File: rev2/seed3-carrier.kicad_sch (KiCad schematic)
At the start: 84 parts, among them J1 AudioJack2_Switch, J2 AudioJack2, J3 POWER_BOARD, J4 DISPLAY_UART, J5 SJ3-35063AG, J6 Seed3_PINS_RIGHT, J7 Seed3_PINS_LEFT, Q1 AO3401A, Q2 2N7002, Q3 2N7002, Q4 2N7002, SW1 EC11E, U1 TLV9064IDR, U2 TPA6111A2DR, U3 SN74LVC1G123DCTR

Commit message: Add J8 internal line out to the speaker amp
- Add J8, a 2-pin JST-XH (B2B-XH-A): pin 1 on J2's tip after R3,
  now named LINE_OUT, and pin 2 on GND. It feeds the speaker amp on
  the power board or a class D module while prototyping.
- Keep J2 as an external line out on the same net.
- Document J8, cabling and speaker wiring in rev2/CHANGES.md.

Co-Authored-By: Claude Opus 5.5 <noreply@anthropic.com>
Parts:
- added J8: LINE_OUT, Connector_JST:JST_XH_B2B-XH-A_1x02_P2.50mm_Vertical, symbol Connector_Generic:Conn_01x02
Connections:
- net GND: now also J8.2 (Pin_2)
- net LINE_OUT: now reaches J2.T, R3.1, R4.2
- net LINE_OUT: now also J8.1 (Pin_1)
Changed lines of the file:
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@@
+		)
+	)
+	(wire
+		(pts
+			(xy 223.52 43.18) (xy 223.52 38.1)
+		)
+		(stroke
+			(width 0)
+			(type default)
+		)
+	)
+	(label "LINE_OUT"
+		(at 223.52 38.1 90)
+		(effects
+			(font
+				(size 1.27 1.27)
+			)
+			(justify left bottom)
+		)
+	)
+	(symbol
+		(lib_id "Connector_Generic:Conn_01x02")
+		(at 264.16 48.26 0)
+		(unit 1)
+		(body_style 1)
+		(exclude_from_sim no)
+		(in_bom yes)
+		(on_board yes)
+		(in_pos_files yes)
+		(dnp no)
+		(property "Reference" "J8"
+			(at 264.16 45.72 0)
+			(show_name no)
+			(do_not_autoplace no)
+			(effects
+				(font
+					(size 1.27 1.27)
+				)
+				(justify left)
+			)
+		)
+		(property "Value" "LINE_OUT"
+			(at 264.16 53.34 0)
+			(show_name no)
+			(do_not_autoplace no)
+			(effects
+				(font
+					(size 1.27 1.27)
+				)
+				(justify left)
+			)
+		)
+		(property "Footprint" "Connector_JST:JST_XH_B2B-XH-A_1x02_P2.50mm_Vertical"
+			(at 264.16 48.26 0)
+			(hide yes)
+			(show_name no)
+			(do_not_autoplace no)
+			(effects
+				(font
+					(size 1.27 1.27)
+				)
+			)
+		)
+		(property "Datasheet" ""
+			(at 264.16 48.26 0)
+			(hide yes)
+			(show_name no)
+			(do_not_autoplace no)
+			(effects
+				(font
+					(size 1.27 1.27)
+				)
+			)
+		)
+		(property "Description" "Generic connector, single row, 01x02, script generated (kicad-library-utils/schlib/autogen/connector/)"
+			(at 264.16 48.26 0)
+			(hide yes)
+			(show_name no)
+			(do_not_autoplace no)
+			(effects
+				(font
+					(size 1.27 1.27)
+				)
+			)
+		)
+		(pin "1"
+		)
+		(pin "2"
+		)
+		(pin "4")
+		(instances
+			(project "seed3-carrier"
+				(path "/94ecceca-f8ce-4e68-9c84-99ac5115dfb9"
+					(reference "J8")
+					(unit 1)
+				)
+			)
+		)
+	)
+	(label "LINE_OUT"
+		(at 259.08 48.26 180)
+		(effects
+			(font
+				(size 1.27 1.27)
+			)
+			(justify right bottom)
+		)
+	)
+	(wire
+		(pts
+			(xy 259.08 50.8) (xy 256.54 50.8)
+		)
+		(stroke
+			(width 0)
+			(type default)
+		)
+	)
+	(wire
+		(pts
+			(xy 256.54 50.8) (xy 256.54 53.34)
+		)
+		(stroke
+			(width 0)
+			(type default)
+		)
+	)
+	(symbol
+		(lib_id "power:GND")
+		(at 256.54 53.34 0)
+		(unit 1)
+		(body_style 1)
+		(exclude_from_sim no)
+		(in_bom yes)
+		(on_board yes)
+		(in_pos_files yes)
+		(dnp no)
+		(property "Reference" "#PWR058"
+			(at 256.54 53.34 0)
+			(hide yes)
+			(show_name no)
+			(do_not_autoplace no)
+			(effects
+				(font
+					(size 1.27 1.27)
+				)
+			)
+		)
+		(property "Value" "GND"
+			(at 256.54 58.42 0)
+			(show_name no)
+			(do_not_autoplace no)
+			(effects
+				(font
+					(size 1.27 1.27)
+				)
+			)
+		)
+		(property "Footprint" ""
+			(at 256.54 53.34 0)
+			(hide yes)
+			(show_name no)
+			(do_not_autoplace no)
+			(effects
+				(font
+					(size 1.27 1.27)
+				)
+			)
+		)
+		(property "Datasheet" ""
+			(at 256.54 53.34 0)
+			(hide yes)
+			(show_name no)
+			(do_not_autoplace no)
+			(effects
+				(font
+					(size 1.27 1.27)
+				)
+			)
+		)
+		(property "Description" "Power symbol creates a global label with name \"GND\" , ground"
+			(at 256.54 53.34 0)
+			(hide yes)
+			(show_name no)
+			(do_not_autoplace no)
+			(effects
+				(font
+					(size 1.27 1.27)
+				)
+			)
+		)
+		(pin "1"
+		)
+		(instances
+			(project "seed3-carrier"
+				(path "/94ecceca-f8ce-4e68-9c84-99ac5115dfb9"
+					(reference "#PWR058")
+					(unit 1)
+				)
+			)
 		)
 	)

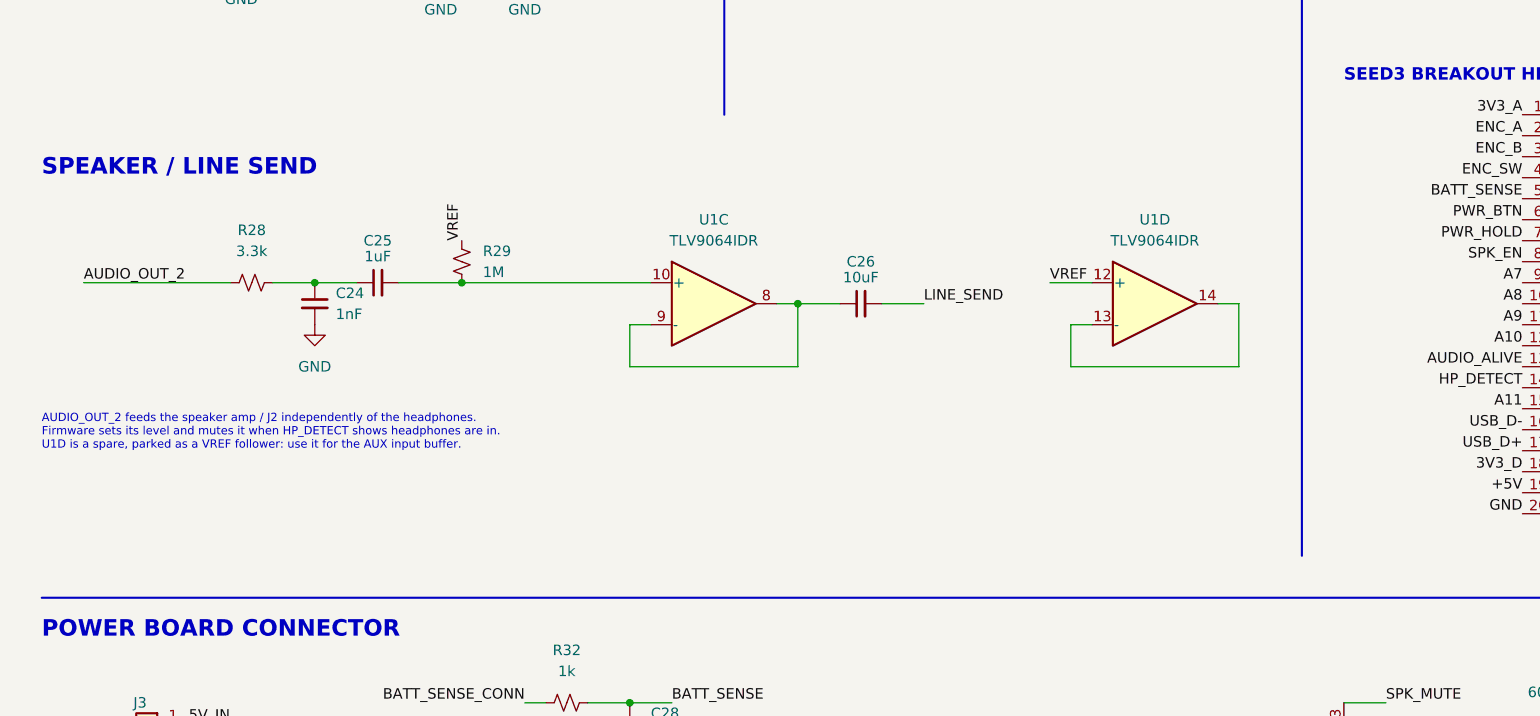
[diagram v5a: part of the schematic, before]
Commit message: Add the AUX input on J9 through U1D to AUDIO_IN_2
- Add J9, a second SJ3-35063AG 3.5 mm TRS jack. Its detect switch
  is not connected.
- Sum tip and ring to mono with R40/R41 (10k), hold the node with
  R38 (47k) and C31 (1nF), AC-couple with C32 (1uF) biased to VREF
  by R39 (100k), then R42 (1k) into the U1D follower driving
  AUDIO_IN_2.
- Remove U1D's VREF-follower parking and move it next to the AUX
  parts. Rename the section to "Speaker / line send, AUX input".
- Document the path, firmware mixing and the level check in
  rev2/CHANGES.md.

Co-Authored-By: Claude Opus 5.5 <noreply@anthropic.com>
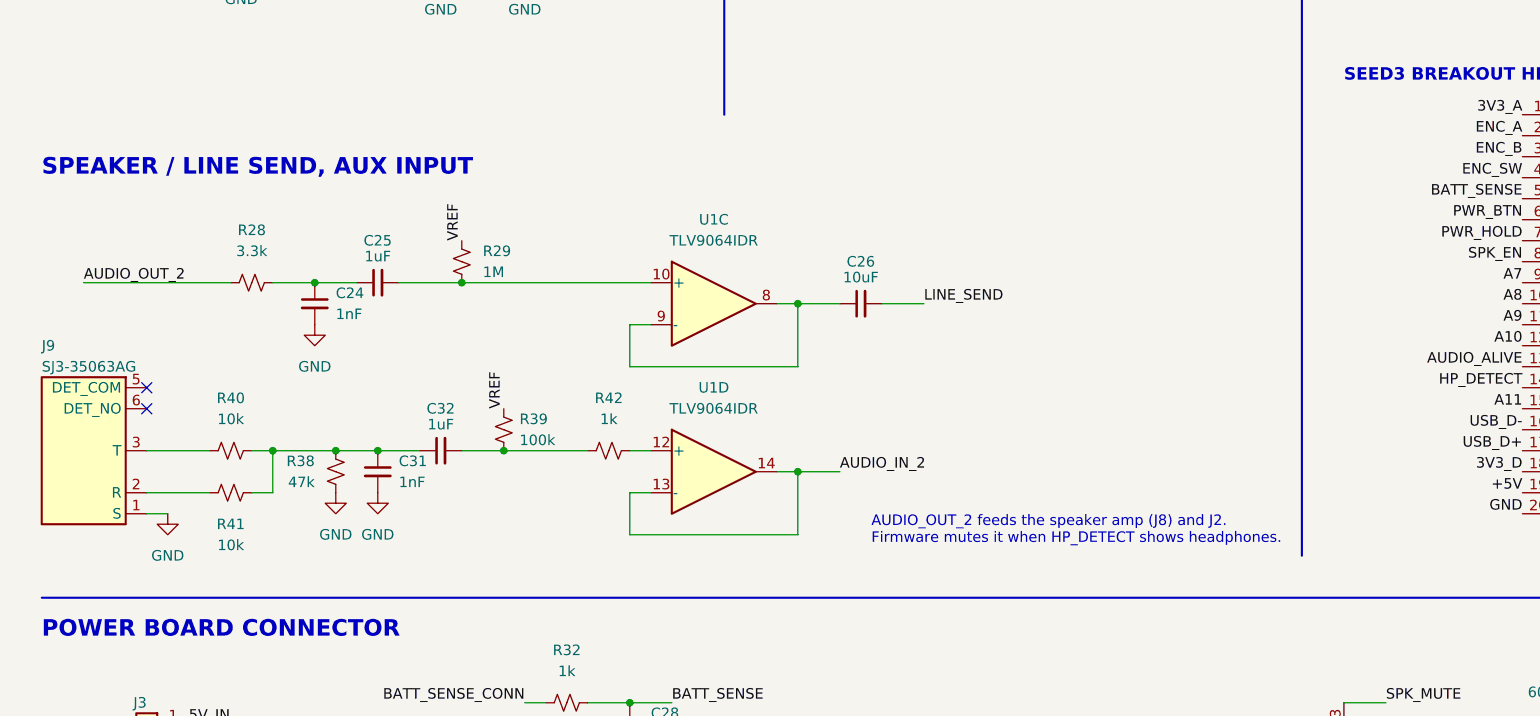
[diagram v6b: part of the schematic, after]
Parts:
- added C31: 1nF, Capacitor_SMD:C_1206_3216Metric_Pad1.33x1.80mm_HandSolder, symbol Device:C_Small
- added C32: 1uF, Capacitor_SMD:C_1206_3216Metric_Pad1.33x1.80mm_HandSolder, symbol Device:C_Small
- added J9: SJ3-35063AG, Seed3_Carrier:Jack_3.5mm_SameSky_SJ3-35063AG_Horizontal, symbol seed3-carrier:SJ3-35063AG
- added R38: 47k, Resistor_SMD:R_1206_3216Metric_Pad1.30x1.75mm_HandSolder, symbol Device:R_Small_US
- added R39: 100k, Resistor_SMD:R_1206_3216Metric_Pad1.30x1.75mm_HandSolder, symbol Device:R_Small_US
- added R40, R41: 10k, Resistor_SMD:R_1206_3216Metric_Pad1.30x1.75mm_HandSolder, symbol Device:R_Small_US
- added R42: 1k, Resistor_SMD:R_1206_3216Metric_Pad1.30x1.75mm_HandSolder, symbol Device:R_Small_US
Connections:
- net AUDIO_IN_2: now also U1.13 (-), U1.14
- net GND: now also C31.2, J9.1 (S), R38.2
- net VREF: now also R39.1; no longer U1.12 (+)
- new net: J9.2 (R), R41.1
- new net: C31.1, C32.1, R38.1, R40.2, R41.2
- new net: J9.3 (T), R40.1
- new net: C32.2, R39.2, R42.1
- new net: R42.2, U1.12 (+)
- no-connect marks 1 -> 3
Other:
- note added: "AUDIO_OUT_2 feeds the speaker amp (J8) and J2. Firmware mutes it when HP_DETECT shows headphones."
- note added: "SPEAKER / LINE SEND, AUX INPUT"
- note removed: "AUDIO_OUT_2 feeds the speaker amp / J2 independently of the headphones. Firmware sets its level and mutes it when HP_DETECT shows headphones are in. U1D is a spare, parked as a VREF follower: use it for the AUX input buffer."
- note removed: "SPEAKER / LINE SEND"
- moved on the sheet: U1D

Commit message: Apply rev 2 schematic design review fixes
Technical:
- R32 1k -> 10k so the power board's battery divider cannot
  back-power an unpowered Daisy through BATT_SENSE.
- R13/R14 100R -> 1k: now only bleed resistors for C14/C15 since
  the rev 1 tip-switch line out is gone.
- Add R43/R44 (1k) in series with the display UART. J4 now carries
  UART_TX_CONN/UART_RX_CONN.

Style:
- Add voltage ratings to C7, C9, C26 and C30. Rename TP9 to TP_5V.
- Rename "Audio output" to "Headphone buffer" and update the Q1,
  op-amp rail and watchdog notes. Update the title block date.
- Move C9's labels clear of the PWR_FLAG symbols.
- Record the fixes and the BATT_SENSE power board requirement in
  rev2/CHANGES.md.

Co-Authored-By: Claude Opus 5.5 <noreply@anthropic.com>
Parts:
- added R43, R44: 1k, Resistor_SMD:R_1206_3216Metric_Pad1.30x1.75mm_HandSolder, symbol Device:R_Small_US
- C26, C9: value 10uF -> 10uF 16V
- C30: value 47uF -> 47uF 16V
- C7: value 47uF -> 47uF 10V
- R13, R14: value 100 -> 1k
- R32: value 1k -> 10k
- TP9: value TP_AMP_5V -> TP_5V
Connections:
- net DISPLAY_UART_RX: now also R44.2; no longer J4.3 (Pin_3)
- net DISPLAY_UART_TX: now also R43.1; no longer J4.2 (Pin_2)
- new net UART_RX_CONN: J4.3 (Pin_3), R44.1
- new net UART_TX_CONN: J4.2 (Pin_2), R43.2
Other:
- note added: "HEADPHONE BUFFER"
- note added: "Op-amp power rails"
- note added: "Q1: reverse-polarity protection for 5V_IN (J3)"
- note added: "U2 stays muted (SHUTDOWN pulled to +5V) unless the firmware toggles AUDIO_ALIVE from the audio callback. Each rising edge retriggers U3; if edges stop for ~10 ms (Rext x Cext), Q (WD_OK) falls: Q2 mutes U2 and Q3 mutes the speaker amp. Also muted while the Daisy is absent, booting or in DFU (B is held low). The speaker amp mute is SPK_MUTE on J3."
- note removed: "AUDIO OUTPUT"
- note removed: "MOSFET is reverse polarity protection"
- note removed: "OPAMP power rails"
- note removed: "U2 stays muted (SHUTDOWN pulled to +5V) unless the firmware toggles AUDIO_ALIVE from the audio callback. Each rising edge retriggers U3; if edges stop for ~10 ms (Rext x Cext), Q falls, Q2 turns off and the amps mute. Also muted while the Daisy is absent, booting or in DFU (B is held low). AMP_SHUTDOWN mutes U2; the speaker amp uses SPK_MUTE on J3."

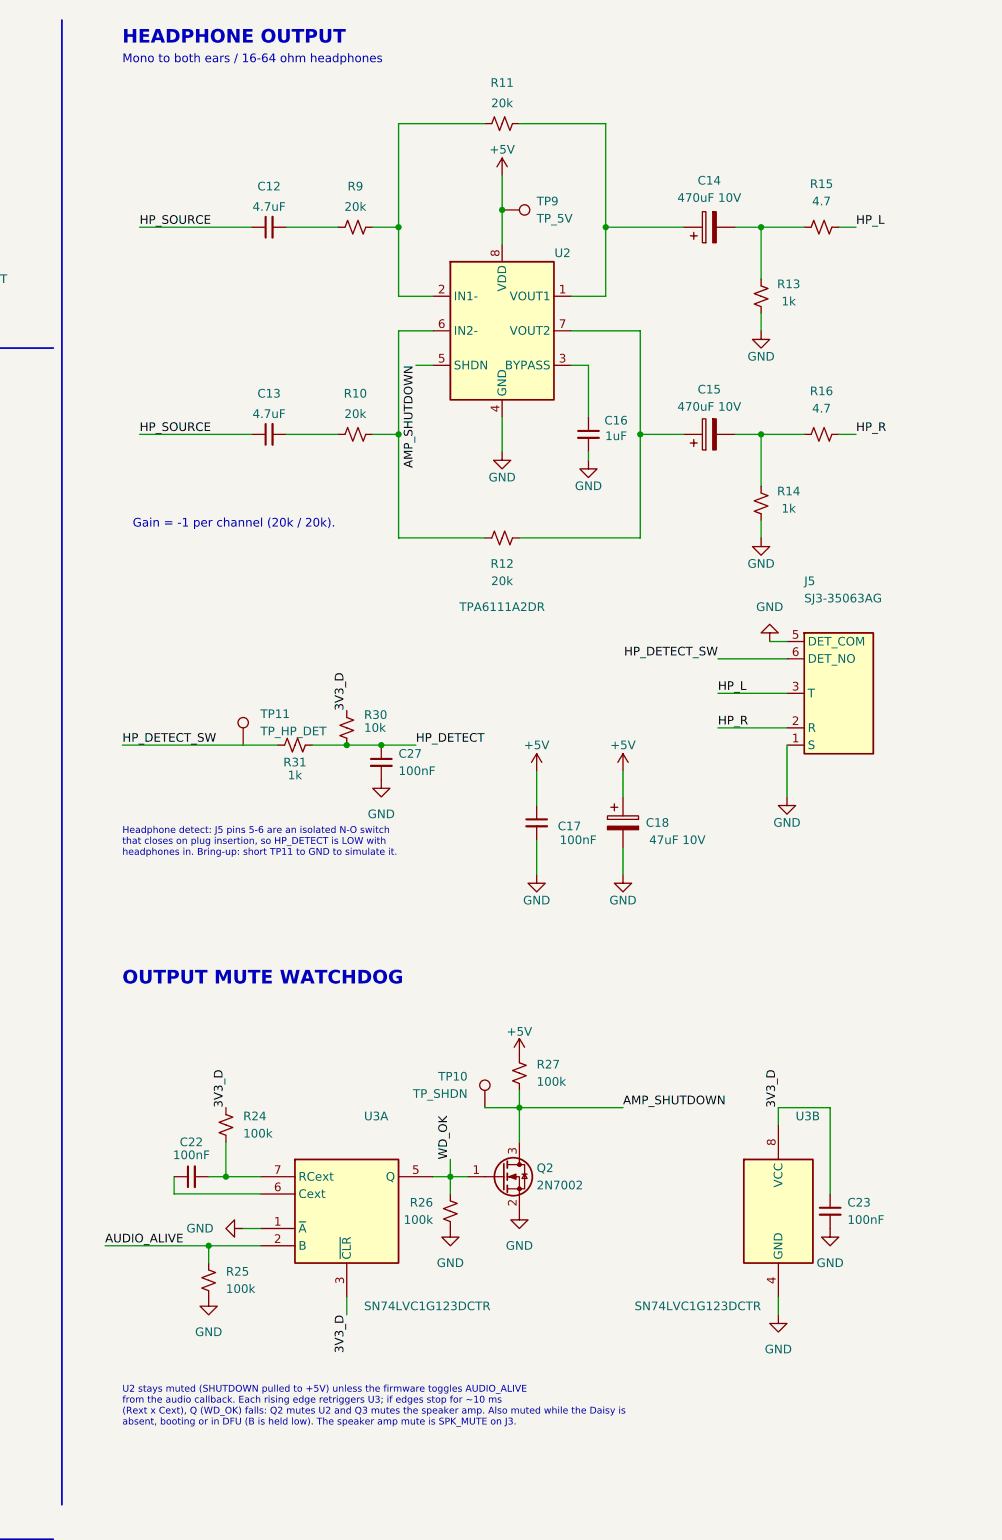
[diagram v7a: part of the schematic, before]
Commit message: Replace the TPA6111A2 headphone amp with a TPA6132A2
- U2 is now a TPA6132A2RTE DirectPath amp (WQFN-16). Its outputs sit
  at 0 V and drive J5 directly.
- Remove C14/C15 (470uF output caps), R9-R16, C16, Q2 and R27.
- Add C33 (VDD), C34 (HPVDD), C35 (flying) and C36 (HPVSS) per the
  datasheet. Inputs are single ended through C12/C13, and gain is
  0 dB (G0 high, G1 low).
- Drive U2's active-high EN straight from WD_OK, replacing
  AMP_SHUTDOWN. Move TP10 onto WD_OK.
- Add a TPA6132A2RTE symbol with pins arranged for this circuit to
  seed3-carrier.kicad_sym.
- Update rev2/CHANGES.md: the watchdog, the power connector and
  firmware notes, open items, and a new section for the swap.

Co-Authored-By: Claude Opus 5.5 <noreply@anthropic.com>
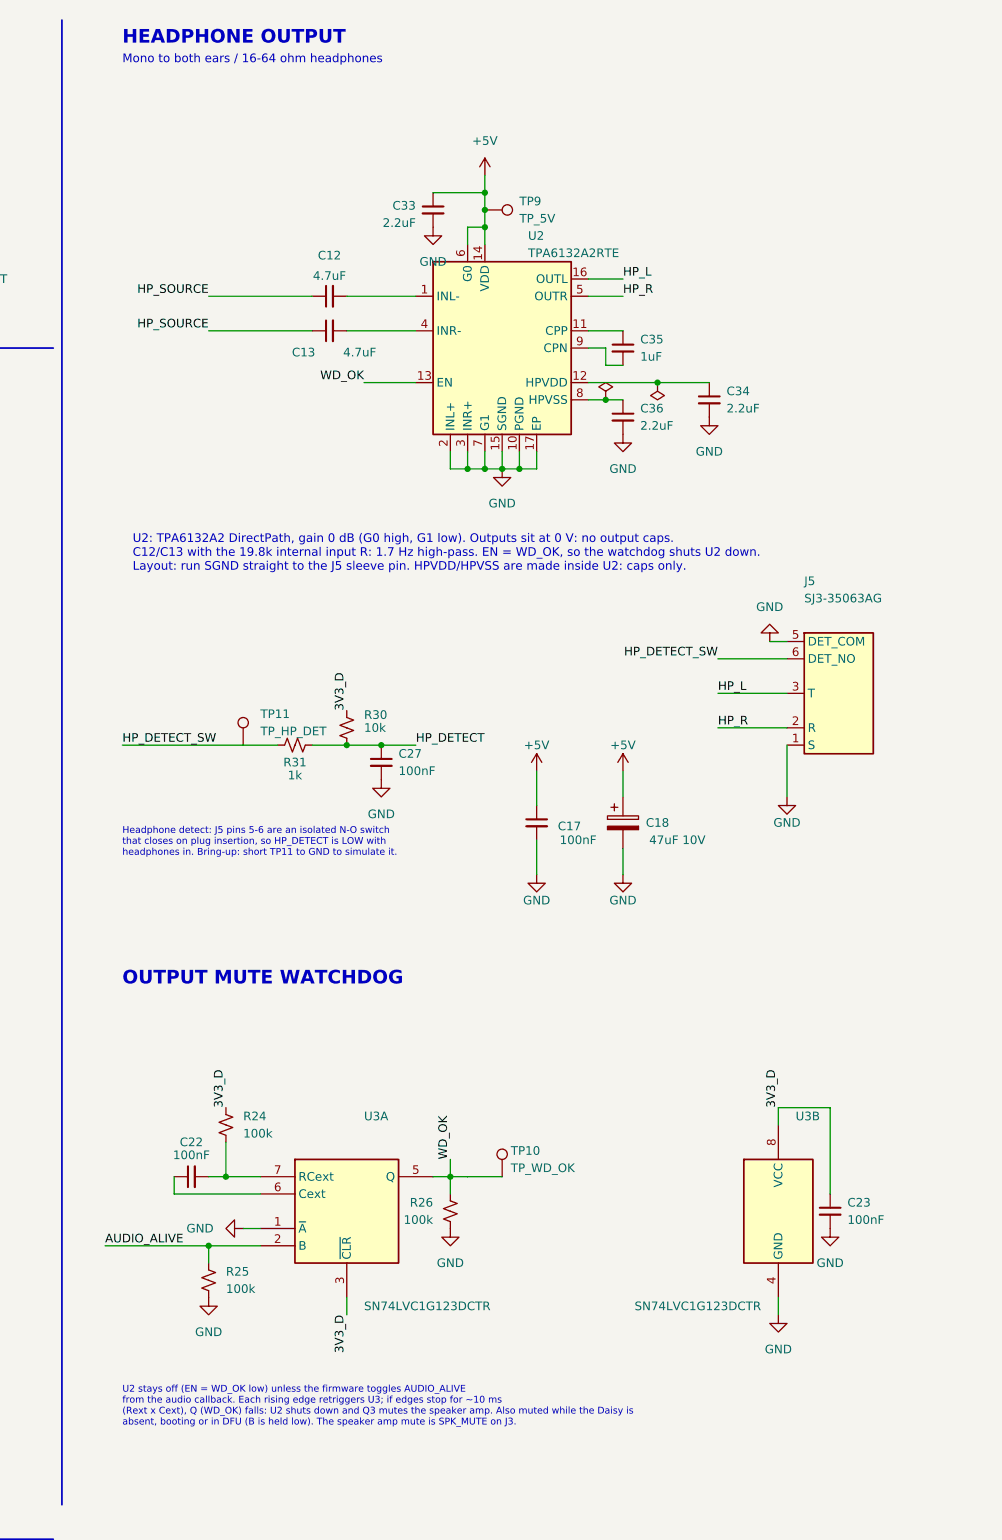
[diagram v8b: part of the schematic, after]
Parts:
- removed C14, C15: 470uF 10V, Capacitor_THT:CP_Radial_D8.0mm_P3.50mm, symbol Device:C_Polarized
- removed C16: 1uF, Capacitor_SMD:C_1206_3216Metric_Pad1.33x1.80mm_HandSolder, symbol Device:C_Small
- removed Q2: 2N7002, Package_TO_SOT_SMD:SOT-23, symbol Transistor_FET:2N7002
- removed R10, R11, R12, R9: 20k, Resistor_SMD:R_1206_3216Metric_Pad1.30x1.75mm_HandSolder, symbol Device:R_Small_US
- removed R13, R14: 1k, Resistor_SMD:R_1206_3216Metric_Pad1.30x1.75mm_HandSolder, symbol Device:R_Small_US
- removed R15, R16: 4.7, Resistor_SMD:R_1206_3216Metric_Pad1.30x1.75mm_HandSolder, symbol Device:R_Small_US
- removed R27: 100k, Resistor_SMD:R_1206_3216Metric_Pad1.30x1.75mm_HandSolder, symbol Device:R_Small_US
- removed U2: TPA6111A2DR, Package_SO:SOIC-8_3.9x4.9mm_P1.27mm, symbol seed3-carrier:TPA6111A2DR
- added C33, C34, C36: 2.2uF, Capacitor_SMD:C_0805_2012Metric_Pad1.18x1.45mm_HandSolder, symbol Device:C_Small
- added C35: 1uF, Capacitor_SMD:C_0805_2012Metric_Pad1.18x1.45mm_HandSolder, symbol Device:C_Small
- added U2: TPA6132A2RTE, Package_DFN_QFN:WQFN-16-1EP_3x3mm_P0.5mm_EP1.6x1.6mm_ThermalVias, symbol seed3-carrier:TPA6132A2RTE
- TP10: value TP_SHDN -> TP_WD_OK
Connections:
- net AMP_SHUTDOWN is gone; now on net WD_OK: TP10.1
- net +5V: now also C33.1, U2.14 (VDD), U2.6 (G0)
- net GND: now also C33.2, C34.2, C36.2, U2.10 (PGND), U2.15 (SGND), U2.17 (EP), U2.2 (INL+), U2.3 (INR+), U2.7 (G1)
- net HP_L: now also U2.16 (OUTL)
- net HP_R: now also U2.5 (OUTR)
- net WD_OK: now also U2.13 (EN)
- net at C12.2: now also U2.1 (INL-)
- net at C13.2: now also U2.4 (INR-)
- new net: C35.1, U2.11 (CPP)
- new net: C34.1, U2.12 (HPVDD)
- new net: C36.1, U2.8 (HPVSS)
- new net: C35.2, U2.9 (CPN)
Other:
- note added: "U2 stays off (EN = WD_OK low) unless the firmware toggles AUDIO_ALIVE from the audio callback. Each rising edge retriggers U3; if edges stop for ~10 ms (Rext x Cext), Q (WD_OK) falls: U2 shuts down and Q3 mutes the speaker amp. Also muted while the Daisy is absent, booting or in DFU (B is held low). The speaker amp mute is SPK_MUTE on J3."
- note added: "U2: TPA6132A2 DirectPath, gain 0 dB (G0 high, G1 low). Outputs sit at 0 V: no output caps. C12/C13 with the 19.8k internal input R: 1.7 Hz high-pass. EN = WD_OK, so the watchdog shuts U2 down. Layout: run SGND straight to the J5 sleeve pin. HPVDD/HPVSS are made inside U2: caps only."
- note removed: "Gain = -1 per channel (20k / 20k)."
- note removed: "U2 stays muted (SHUTDOWN pulled to +5V) unless the firmware toggles AUDIO_ALIVE from the audio callback. Each rising edge retriggers U3; if edges stop for ~10 ms (Rext x Cext), Q (WD_OK) falls: Q2 mutes U2 and Q3 mutes the speaker amp. Also muted while the Daisy is absent, booting or in DFU (B is held low). The speaker amp mute is SPK_MUTE on J3."
- moved on the sheet: C12, C13, TP10, TP9
